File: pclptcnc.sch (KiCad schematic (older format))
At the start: 248 parts, among them P1 ARK825A-3, P3 ARK825A-4, P4 ARK825A-3, P5 ARK825A-3, P6 ARK825A-3, P7 ARK825A-3, P8 ARK825A-3, Q1 BC807-40, Q10 BC807-40, Q11 BC807-40, Q12 BC807-40, Q13 BC807-40, Q14 BC807-40, Q15 BC807-40, Q16 BC807-40, Q17 BC807-40, Q18 BC807-40, Q2 BC807-40, Q3 BC807-40, Q4 BC807-40, Q5 BC807-40, Q6 BC807-40, Q7 BC807-40, Q8 BC807-40, Q9 BC807-40, U1 74LVC1G3157GW, U10 SN74LVC2G17, U11 74HCT14, U12 SN74LVC2G17, U13 74HCT14, U2 HCPL2630, U3 HCPL2630, U4 HCPL2630, U5 HCPL2630, U6 HCPL2630, U7 HCPL2630, U8 74HCT14, U9 74HCT14, j1 DB25, j2 DB25

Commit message: merged all libraries
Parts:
- R1, R10, R100, R101, R102, R103, R104, R105, R106, R107, R108, R109, R11, R110, R111, R112, R113, R114, R115, R116, R117, R118, R119, R12, R120, R121, R122, R123, R13, R14, R15, R16, R17, R18, R19, R2, R20, R21, R22, R23, R24, R25, R26, R27, R28, R29, R3, R30, R31, R32, R33, R34, R35, R36, R37, R38, R39, R4, R40, R41, R42, R43, R44, R45, R46, R47, R48, R49, R5, R50, R51, R52, R53, R54, R55, R56, R57, R58, R59, R6, R60, R61, R62, R63, R64, R65, R66, R67, R68, R69, R7, R70, R71, R72, R73, R74, R75, R76, R77, R78, R79, R8, R80, R81, R82, R83, R84, R85, R86, R87, R88, R89, R9, R90, R91, R92, R93, R94, R95, R96, R97, R98, R99, R_LED1, R_LED10, R_LED11, R_LED12, R_LED13, R_LED14, R_LED15, R_LED16, R_LED17, R_LED18, R_LED19, R_LED2, R_LED20, R_LED3, R_LED4, R_LED5, R_LED6, R_LED7, R_LED8, R_LED9: symbol R -> R_SFP

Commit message: futher library development
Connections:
- no-connect marks 5 -> 7
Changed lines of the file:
@@
 LIBS:valves
 LIBS:new_lib
+LIBS:pclptcnc-cache
 EELAYER 27 0
 EELAYER END
@@
 Sheet 1 1
 Title ""
-Date "1 nov 2013"
+Date "2 nov 2013"
 Rev ""
 Comp ""
@@
 Text Label 19050 6250 0    60   ~ 0
 SENSOR_4
-Text Label 5950 1950 2    60   ~ 0
+Text Label 5950 2000 2    60   ~ 0
 SENSOR_2
 Text Label 10150 2300 0    60   ~ 0
@@
 Text Label 2650 1750 2    60   ~ 0
 RC1
-Text Label 2650 1550 2    60   ~ 0
+Text Label 2650 1500 2    60   ~ 0
 RC2
-Text Label 2650 1950 2    60   ~ 0
+Text Label 2650 2000 2    60   ~ 0
 RC3
-Text Label 2650 2150 2    60   ~ 0
+Text Label 2650 2250 2    60   ~ 0
 RC4
 Text Label 2650 3550 2    60   ~ 0
 RC5
-Text Label 2650 3350 2    60   ~ 0
+Text Label 2650 3300 2    60   ~ 0
 RC6
-Text Label 2650 3750 2    60   ~ 0
+Text Label 2650 3800 2    60   ~ 0
 RC7
-Text Label 2650 3950 2    60   ~ 0
+Text Label 2650 4050 2    60   ~ 0
 RC8
-Text Label 2650 5150 2    60   ~ 0
+Text Label 2650 5100 2    60   ~ 0
 RC9
-Text Label 2650 5550 2    60   ~ 0
+Text Label 2650 5600 2    60   ~ 0
 RC10
 Text Label 2650 5350 2    60   ~ 0
 RC11
-Text Label 2650 5750 2    60   ~ 0
-RC12
 Text Label 2650 5850 2    60   ~ 0
+RC12
+Text Label 2650 5950 2    60   ~ 0
 PC12
 Text Label 2650 5450 2    60   ~ 0
 PC11
-Text Label 2650 5650 2    60   ~ 0
+Text Label 2650 5700 2    60   ~ 0
 PC10
-Text Label 2650 5250 2    60   ~ 0
+Text Label 2650 5200 2    60   ~ 0
 PC9
-Text Label 2650 4050 2    60   ~ 0
+Text Label 2650 4150 2    60   ~ 0
 PC8
-Text Label 2650 3850 2    60   ~ 0
+Text Label 2650 3900 2    60   ~ 0
 PC7
-Text Label 2650 3450 2    60   ~ 0
+Text Label 2650 3400 2    60   ~ 0
 PC6
 Text Label 2650 3650 2    60   ~ 0
 PC5
-Text Label 2650 2250 2    60   ~ 0
+Text Label 2650 2350 2    60   ~ 0
 PC4
-Text Label 2650 2050 2    60   ~ 0
+Text Label 2650 2100 2    60   ~ 0
 PC3
-Text Label 2650 1650 2    60   ~ 0
+Text Label 2650 1600 2    60   ~ 0
 PC2
 Text Label 2650 1850 2    60   ~ 0
@@
 Text Label 5400 9550 0    60   ~ 0
 GND
-Text Label 5950 9950 0    60   ~ 0
+Text Label 6000 9950 0    60   ~ 0
 VCC
 Text Notes 19650 1150 0    60   ~ 0
@@
 Text Label 21900 1450 0    60   ~ 0
 GND
-Text Label 21900 1950 0    60   ~ 0
+Text Label 21900 1550 0    60   ~ 0
 PC_IN1
 Text Label 21900 1750 0    60   ~ 0
 PC_IN2
-Text Label 21900 1550 0    60   ~ 0
+Text Label 21900 1950 0    60   ~ 0
 PC_IN3
 Text Label 21900 1350 0    60   ~ 0
@@
 Text Label 20400 6250 0    60   ~ 0
 SENSOR_5
-Text Label 5950 1550 2    60   ~ 0
+Text Label 5950 1500 2    60   ~ 0
 SENSOR_4
-Text Label 5950 2150 2    60   ~ 0
+Text Label 5950 2250 2    60   ~ 0
 SENSOR_1
 Text Label 20100 5950 0    60   ~ 0
@@
 Text Label 13050 2600 0    60   ~ 0
 ISOLATED_GND
-Text Label 13050 1700 0    60   ~ 0
-ISOLATED_VCC
 $Comp
 L HCPL2630 U4
@@
 Text Notes 16950 4350 0    60   ~ 0
 OUTPUT CONNECTORS
-Text Label 6150 7050 0    60   ~ 0
+Text Label 6250 7050 0    60   ~ 0
 ISOLATED_VCC
-Text Label 5350 7450 0    60   ~ 0
+Text Label 5300 7450 0    60   ~ 0
 ISOLATED_GND
 Text Label 10250 6500 0    60   ~ 0
@@
 	18800 5300 18800 4900
 Wire Wire Line
-	19050 4500 18550 4500
+	18550 4500 19050 4500
 Wire Wire Line
 	18750 5650 18750 5850
@@
 	21500 5300 21500 4900
 Wire Wire Line
-	21750 4500 21250 4500
+	21250 4500 21750 4500
 Wire Wire Line
 	21450 5650 21450 5850
@@
 	20150 5300 20150 4900
 Wire Wire Line
-	20400 4500 19900 4500
+	19900 4500 20400 4500
 Wire Wire Line
 	20100 5650 20100 5850
@@
 	18800 7050 18800 6650
 Wire Wire Line
-	19050 6250 18550 6250
+	18550 6250 19050 6250
 Wire Wire Line
 	18750 7400 18750 7600
@@
 	20150 7050 20150 6650
 Wire Wire Line
-	20400 6250 19900 6250
+	19900 6250 20400 6250
 Wire Wire Line
 	20100 7400 20100 7600
@@
 	5150 7050 5450 7050
 Wire Wire Line
-	5400 9550 6600 9550
+	6600 9550 5400 9550
 Connection ~ 6200 9550
 Wire Wire Line
-	6600 9550 6600 8850
+	6600 8850 6600 9550
 Connection ~ 6600 9200
 Wire Wire Line
@@
 Connection ~ 7000 9550
 Connection ~ 6600 9950
-Wire Wire Line
-	5200 9950 5200 9550
 Connection ~ 6200 9950
 Wire Wire Line
@@
 Text Label 20250 3650 0    60   ~ 0
 SENSOR_5
-Text Label 5200 9950 0    60   ~ 0
-VCC_NFused
-$Comp
-L FUSE_N F1
-U 1 1 523251F3
-P 5700 7050
-F 0 "F1" H 5800 7100 40  0000 C CNN
-F 1 "FUSE 1A" H 5600 7000 40  0000 C CNN
-F 2 "~" H 5700 7050 60  0000 C CNN
-F 3 "~" H 5700 7050 60  0000 C CNN
-	1    5700 7050
-	1    0    0    -1
-$EndComp
-$Comp
-L FUSE_N F2
-U 1 1 523253C0
-P 5700 9950
-F 0 "F2" H 5800 10000 40  0000 C CNN
-F 1 "FUSE 0.5A" H 5600 9900 40  0000 C CNN
-F 2 "~" H 5700 9950 60  0000 C CNN
-F 3 "~" H 5700 9950 60  0000 C CNN
-	1    5700 9950
-	1    0    0    -1
-$EndComp
-Text Label 5200 7050 0    60   ~ 0
+Text Label 5150 7050 0    60   ~ 0
 ISOLATED_VCC_NFused
 NoConn ~ 5150 7250
-Text Label 5950 2250 2    60   ~ 0
+Text Label 5950 2350 2    60   ~ 0
 GND
 Text Label 5950 3550 2    60   ~ 0
@@
 Text Label 5700 5950 0    60   ~ 0
 IOSRCTR_BASE
-Text Label 5950 2050 2    60   ~ 0
+Text Label 5950 2100 2    60   ~ 0
 GND
 Text Label 5950 1850 2    60   ~ 0
 GND
-Text Label 5950 1650 2    60   ~ 0
+Text Label 5950 1600 2    60   ~ 0
 GND
 $Comp
@@
 Text Label 10100 11500 2    60   ~ 0
 SRC_SEL
+Text Label 5250 9950 0    60   ~ 0
+VCC_NFused
+Wire Wire Line
+	5200 9950 5200 9550
+NoConn ~ 12100 10750
+NoConn ~ 12100 10950
+Text Label 13050 1700 0    60   ~ 0
+ISOLATED_VCC
+$Comp
+L FUSE_N F1
+U 1 1 52754D48
+P 5700 7050
+F 0 "F1" H 5800 7100 40  0000 C CNN
+F 1 "FUSE 1A" H 5600 7000 40  0000 C CNN
+F 2 "~" H 5700 7050 60  0000 C CNN
+F 3 "~" H 5700 7050 60  0000 C CNN
+	1    5700 7050
+	1    0    0    -1
+$EndComp
+$Comp
+L FUSE_N F2
+U 1 1 52754D55
+P 5700 9950
+F 0 "F2" H 5800 10000 40  0000 C CNN
+F 1 "FUSE 0.5A" H 5600 9900 40  0000 C CNN
+F 2 "~" H 5700 9950 60  0000 C CNN
+F 3 "~" H 5700 9950 60  0000 C CNN
+	1    5700 9950
+	1    0    0    -1
+$EndComp
 $EndSCHEMATC

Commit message: 05.11.1305.11.1305.11.1305.11.1305.11.13
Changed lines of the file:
@@
 Text Label 5950 3850 2    60   ~ 0
 SENSOR_5
-Text Label 5950 1750 2    60   ~ 0
+Text Label 5950 2000 2    60   ~ 0
 SENSOR_3
 Text Label 19050 6250 0    60   ~ 0
 SENSOR_4
-Text Label 5950 2000 2    60   ~ 0
+Text Label 5950 1750 2    60   ~ 0
 SENSOR_2
 Text Label 10150 2300 0    60   ~ 0
@@
 Text Label 19200 9800 0    60   ~ 0
 PC12
-Text Label 2650 1750 2    60   ~ 0
+Text Label 2650 2000 2    60   ~ 0
 RC1
 Text Label 2650 1500 2    60   ~ 0
 RC2
-Text Label 2650 2000 2    60   ~ 0
+Text Label 2650 1750 2    60   ~ 0
 RC3
 Text Label 2650 2250 2    60   ~ 0
@@
 Text Label 2650 2350 2    60   ~ 0
 PC4
-Text Label 2650 2100 2    60   ~ 0
+Text Label 2650 1850 2    60   ~ 0
 PC3
 Text Label 2650 1600 2    60   ~ 0
 PC2
-Text Label 2650 1850 2    60   ~ 0
+Text Label 2650 2100 2    60   ~ 0
 PC1
 $Comp

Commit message: huge optocouplers movement
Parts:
- removed MUX1, MUX2, MUX3, MUX4: 74HC158, SO16E, symbol 74LS158
- added MUX1, MUX2, MUX3, MUX4: 74HC158, ~, symbol 74HC158
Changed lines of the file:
@@
 Sheet 1 1
 Title ""
-Date "2 nov 2013"
+Date "5 nov 2013"
 Rev ""
 Comp ""
@@
 Text Label 5950 3850 2    60   ~ 0
 SENSOR_5
-Text Label 5950 2000 2    60   ~ 0
+Text Label 5950 1950 2    60   ~ 0
 SENSOR_3
 Text Label 19050 6250 0    60   ~ 0
@@
 $EndComp
 $Comp
-L 74LS158 MUX1
-U 1 1 522E2A35
-P 3400 2050
-F 0 "MUX1" H 3450 2200 60  0000 C CNN
-F 1 "74HC158" H 3450 1900 60  0000 C CNN
-F 2 "SO16E" H 3400 2050 60  0000 C CNN
-F 3 "~" H 3400 2050 60  0000 C CNN
-	1    3400 2050
-	1    0    0    -1
-$EndComp
-$Comp
-L 74LS158 MUX2
-U 1 1 522E2A36
-P 3400 3850
-F 0 "MUX2" H 3450 4000 60  0000 C CNN
-F 1 "74HC158" H 3450 3700 60  0000 C CNN
-F 2 "SO16E" H 3400 3850 60  0000 C CNN
-F 3 "~" H 3400 3850 60  0000 C CNN
-	1    3400 3850
-	1    0    0    -1
-$EndComp
-$Comp
 L 74HCT14 U8
 U 1 1 522E2A37
@@
 Text Label 19200 10800 0    60   ~ 0
 PC7
-Text Label 21850 10800 0    60   ~ 0
-PC8
 Text Label 21850 10600 0    60   ~ 0
+PC8
+Text Label 21850 10800 0    60   ~ 0
 PC9
 Text Label 21850 8800 0    60   ~ 0
@@
 Text Label 19200 9800 0    60   ~ 0
 PC12
-Text Label 2650 2000 2    60   ~ 0
+Text Label 2650 2150 2    60   ~ 0
 RC1
-Text Label 2650 1500 2    60   ~ 0
+Text Label 2650 1950 2    60   ~ 0
 RC2
 Text Label 2650 1750 2    60   ~ 0
 RC3
-Text Label 2650 2250 2    60   ~ 0
+Text Label 2650 1550 2    60   ~ 0
 RC4
-Text Label 2650 3550 2    60   ~ 0
+Text Label 2650 5150 2    60   ~ 0
 RC5
-Text Label 2650 3300 2    60   ~ 0
+Text Label 2650 3350 2    60   ~ 0
 RC6
-Text Label 2650 3800 2    60   ~ 0
+Text Label 2650 3750 2    60   ~ 0
 RC7
-Text Label 2650 4050 2    60   ~ 0
+Text Label 2650 5350 2    60   ~ 0
 RC8
-Text Label 2650 5100 2    60   ~ 0
+Text Label 2650 3550 2    60   ~ 0
 RC9
-Text Label 2650 5600 2    60   ~ 0
+Text Label 2650 5750 2    60   ~ 0
 RC10
-Text Label 2650 5350 2    60   ~ 0
+Text Label 2650 3950 2    60   ~ 0
 RC11
-Text Label 2650 5850 2    60   ~ 0
+Text Label 2650 5550 2    60   ~ 0
 RC12
-Text Label 2650 5950 2    60   ~ 0
+Text Label 2650 4050 2    60   ~ 0
 PC12
-Text Label 2650 5450 2    60   ~ 0
+Text Label 2650 5650 2    60   ~ 0
 PC11
-Text Label 2650 5700 2    60   ~ 0
+Text Label 2650 5850 2    60   ~ 0
 PC10
-Text Label 2650 5200 2    60   ~ 0
+Text Label 2650 5250 2    60   ~ 0
 PC9
-Text Label 2650 4150 2    60   ~ 0
+Text Label 2650 5450 2    60   ~ 0
 PC8
-Text Label 2650 3900 2    60   ~ 0
+Text Label 2650 3850 2    60   ~ 0
 PC7
-Text Label 2650 3400 2    60   ~ 0
+Text Label 2650 3450 2    60   ~ 0
 PC6
 Text Label 2650 3650 2    60   ~ 0
 PC5
-Text Label 2650 2350 2    60   ~ 0
+Text Label 2650 2250 2    60   ~ 0
 PC4
 Text Label 2650 1850 2    60   ~ 0
 PC3
-Text Label 2650 1600 2    60   ~ 0
+Text Label 2650 1650 2    60   ~ 0
 PC2
-Text Label 2650 2100 2    60   ~ 0
+Text Label 2650 2050 2    60   ~ 0
 PC1
 $Comp
@@
 Text Label 6000 6150 3    60   ~ 0
 VCC
-Text Label 15150 9400 2    60   ~ 0
+Text Label 15150 9200 2    60   ~ 0
 RCOUT1
-Text Label 15150 9600 2    60   ~ 0
+Text Label 15150 9000 2    60   ~ 0
 RCOUT2
-Text Label 15150 9800 2    60   ~ 0
-RCOUT3
 Text Label 15150 8800 2    60   ~ 0
+RCOUT3
+Text Label 15150 9400 2    60   ~ 0
 RCOUT4
-Text Label 15150 9000 2    60   ~ 0
+Text Label 15150 9600 2    60   ~ 0
 RCOUT5
-Text Label 15150 9200 2    60   ~ 0
+Text Label 15150 9800 2    60   ~ 0
 RCOUT6
 Text Label 15150 11200 2    60   ~ 0
@@
 Text Label 15150 11600 2    60   ~ 0
 RCOUT9
-Text Label 15150 10600 2    60   ~ 0
+Text Label 15150 11000 2    60   ~ 0
 RCOUT10
 Text Label 15150 10800 2    60   ~ 0
 RCOUT11
-Text Label 15150 11000 2    60   ~ 0
+Text Label 15150 10600 2    60   ~ 0
 RCOUT12
 Text Label 6800 5750 0    60   ~ 0
@@
 Text Label 5700 5550 2    60   ~ 0
 CTRL_SRC
-$Comp
-L 74LS158 MUX3
-U 1 1 522E2A4E
-P 3400 5650
-F 0 "MUX3" H 3450 5800 60  0000 C CNN
-F 1 "74HC158" H 3450 5500 60  0000 C CNN
-F 2 "SO16E" H 3400 5650 60  0000 C CNN
-F 3 "~" H 3400 5650 60  0000 C CNN
-	1    3400 5650
-	1    0    0    -1
-$EndComp
 Text Label 2650 6200 2    60   ~ 0
 GND
@@
 Text Label 17700 10600 2    60   ~ 0
 PC_OUT_A6
-Text Label 17700 11600 2    60   ~ 0
+Text Label 17700 11200 2    60   ~ 0
 PC_OUT_A7
 Text Label 21900 2850 0    60   ~ 0
@@
 Text Label 17700 11400 2    60   ~ 0
 PC_OUT_A8
-Text Label 17700 11200 2    60   ~ 0
+Text Label 17700 11600 2    60   ~ 0
 PC_OUT_A9
 Text Label 20350 8800 2    60   ~ 0
@@
 Text Label 20400 6250 0    60   ~ 0
 SENSOR_5
-Text Label 5950 1500 2    60   ~ 0
+Text Label 5950 1550 2    60   ~ 0
 SENSOR_4
-Text Label 5950 2250 2    60   ~ 0
+Text Label 5950 2150 2    60   ~ 0
 SENSOR_1
 Text Label 20100 5950 0    60   ~ 0
@@
 Text Label 3600 6450 0    60   ~ 0
 GND
-Text Label 4150 1550 0    60   ~ 0
+Text Label 4150 2300 0    60   ~ 0
 FLTRD_SGNL1
-Text Label 4150 2050 0    60   ~ 0
-FLTRD_SGNL2
 Text Label 4150 1800 0    60   ~ 0
+FLTRD_SGNL2
+Text Label 4150 2050 0    60   ~ 0
 FLTRD_SGNL3
-Text Label 4150 2300 0    60   ~ 0
+Text Label 4150 1550 0    60   ~ 0
 FLTRD_SGNL4
 Text Label 4150 3350 0    60   ~ 0
@@
 ISOLATED_VCC_NFused
 NoConn ~ 5150 7250
-Text Label 5950 2350 2    60   ~ 0
+Text Label 5950 2250 2    60   ~ 0
 GND
 Text Label 5950 3550 2    60   ~ 0
@@
 Text Label 5700 5950 0    60   ~ 0
 IOSRCTR_BASE
-Text Label 5950 2100 2    60   ~ 0
+Text Label 5950 2050 2    60   ~ 0
 GND
 Text Label 5950 1850 2    60   ~ 0
 GND
-Text Label 5950 1600 2    60   ~ 0
+Text Label 5950 1650 2    60   ~ 0
 GND
 $Comp
@@
 Text Label 5700 6350 2    60   ~ 0
 GND
-$Comp
-L 74LS158 MUX4
-U 1 1 526D4CB1
-P 6700 2050
-F 0 "MUX4" H 6750 2200 60  0000 C CNN
-F 1 "74HC158" H 6750 1900 60  0000 C CNN
-F 2 "SO16E" H 6700 2050 60  0000 C CNN
-F 3 "~" H 6700 2050 60  0000 C CNN
-	1    6700 2050
-	1    0    0    -1
-$EndComp
 NoConn ~ 21850 11400
 NoConn ~ 20350 11400
@@
 	1    0    0    -1
 $EndComp
+Text Label 5800 9350 0    60   ~ 0
+ISOLATED_VCC
+Text Label 6100 9350 0    60   ~ 0
+ISOLATED_GND
+$Comp
+L 74HC158 MUX1
+U 1 1 5278E1DD
+P 3400 2050
+F 0 "MUX1" H 3450 2200 60  0000 C CNN
+F 1 "74HC158" H 3450 1900 60  0000 C CNN
+F 2 "~" H 3400 2050 60  0000 C CNN
+F 3 "~" H 3400 2050 60  0000 C CNN
+	1    3400 2050
+	1    0    0    -1
+$EndComp
+$Comp
+L 74HC158 MUX2
+U 1 1 5278E1EA
+P 3400 3850
+F 0 "MUX2" H 3450 4000 60  0000 C CNN
+F 1 "74HC158" H 3450 3700 60  0000 C CNN
+F 2 "~" H 3400 3850 60  0000 C CNN
+F 3 "~" H 3400 3850 60  0000 C CNN
+	1    3400 3850
+	1    0    0    -1
+$EndComp
+$Comp
+L 74HC158 MUX3
+U 1 1 5278E1F0
+P 3400 5650
+F 0 "MUX3" H 3450 5800 60  0000 C CNN
+F 1 "74HC158" H 3450 5500 60  0000 C CNN
+F 2 "~" H 3400 5650 60  0000 C CNN
+F 3 "~" H 3400 5650 60  0000 C CNN
+	1    3400 5650
+	1    0    0    -1
+$EndComp
+$Comp
+L 74HC158 MUX4
+U 1 1 5278E1F6
+P 6700 2050
+F 0 "MUX4" H 6750 2200 60  0000 C CNN
+F 1 "74HC158" H 6750 1900 60  0000 C CNN
+F 2 "~" H 6700 2050 60  0000 C CNN
+F 3 "~" H 6700 2050 60  0000 C CNN
+	1    6700 2050
+	1    0    0    -1
+$EndComp

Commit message: близкая компоновка
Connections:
- net FLTRD_SGNL11: now also MUX3.9 (Zd); no longer MUX3.7 (Zb)
- net FLTRD_SGNL12: now also MUX3.7 (Zb); no longer MUX3.9 (Zd)
- net FLTRD_SGNL5: now also MUX2.9 (Zd); no longer MUX2.4 (Za)
- net FLTRD_SGNL6: now also MUX2.7 (Zb); no longer MUX2.12 (Zc)
- net FLTRD_SGNL7: now also MUX2.12 (Zc); no longer MUX2.7 (Zb)
- net FLTRD_SGNL8: now also MUX2.4 (Za); no longer MUX2.9 (Zd)
- net PC12: now also U11.6 (3Y); no longer U10.4 (2Y)
- net PC4: now also U10.4 (2Y); no longer U11.2 (1Y)
- net PC5: now also MUX2.13 (I1c); no longer MUX2.6 (I1b)
- net PC6: now also MUX2.6 (I1b), U11.2 (1Y); no longer MUX2.3 (I1a), U11.6 (3Y)
- net PC7: now also MUX2.3 (I1a); no longer MUX2.13 (I1c)
- net RC11: now also MUX2.2 (I0a); no longer MUX2.11 (I0d)
- net RC6: now also MUX2.14 (I0c); no longer MUX2.2 (I0a)
- net RC7: now also MUX2.11 (I0d); no longer MUX2.14 (I0c)
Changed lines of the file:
@@
 Sheet 1 1
 Title ""
-Date "5 nov 2013"
+Date "6 nov 2013"
 Rev ""
 Comp ""
@@
 Text Label 19200 11600 0    60   ~ 0
 PC3
-Text Label 19200 10600 0    60   ~ 0
+Text Label 19200 9800 0    60   ~ 0
 PC4
 Text Label 21850 11000 0    60   ~ 0
 PC5
-Text Label 19200 11000 0    60   ~ 0
+Text Label 19200 10600 0    60   ~ 0
 PC6
 Text Label 19200 10800 0    60   ~ 0
@@
 Text Label 21850 9800 0    60   ~ 0
 PC11
-Text Label 19200 9800 0    60   ~ 0
+Text Label 19200 11000 0    60   ~ 0
 PC12
 Text Label 2650 2150 2    60   ~ 0
@@
 Text Label 2650 5150 2    60   ~ 0
 RC5
-Text Label 2650 3350 2    60   ~ 0
+Text Label 2650 3750 2    60   ~ 0
 RC6
-Text Label 2650 3750 2    60   ~ 0
+Text Label 2650 3950 2    60   ~ 0
 RC7
 Text Label 2650 5350 2    60   ~ 0
@@
 Text Label 2650 5750 2    60   ~ 0
 RC10
-Text Label 2650 3950 2    60   ~ 0
+Text Label 2650 3350 2    60   ~ 0
 RC11
 Text Label 2650 5550 2    60   ~ 0
@@
 Text Label 2650 5450 2    60   ~ 0
 PC8
+Text Label 2650 3450 2    60   ~ 0
+PC7
+Text Label 2650 3650 2    60   ~ 0
+PC6
 Text Label 2650 3850 2    60   ~ 0
-PC7
-Text Label 2650 3450 2    60   ~ 0
-PC6
-Text Label 2650 3650 2    60   ~ 0
 PC5
 Text Label 2650 2250 2    60   ~ 0
@@
 Text Label 4150 1550 0    60   ~ 0
 FLTRD_SGNL4
+Text Label 4150 4100 0    60   ~ 0
+FLTRD_SGNL5
+Text Label 4150 3600 0    60   ~ 0
+FLTRD_SGNL6
+Text Label 4150 3850 0    60   ~ 0
+FLTRD_SGNL7
 Text Label 4150 3350 0    60   ~ 0
-FLTRD_SGNL5
-Text Label 4150 3850 0    60   ~ 0
-FLTRD_SGNL6
-Text Label 4150 3600 0    60   ~ 0
-FLTRD_SGNL7
-Text Label 4150 4100 0    60   ~ 0
 FLTRD_SGNL8
 Text Label 4150 5150 0    60   ~ 0
@@
 Text Label 4150 5650 0    60   ~ 0
 FLTRD_SGNL10
+Text Label 4150 5900 0    60   ~ 0
+FLTRD_SGNL11
 Text Label 4150 5400 0    60   ~ 0
-FLTRD_SGNL11
-Text Label 4150 5900 0    60   ~ 0
 FLTRD_SGNL12
 Text Label 7450 1800 0    60   ~ 0

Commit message: version 0.2a completed
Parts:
- removed R1: 2K7, SM0805, symbol R_SFP
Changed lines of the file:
@@
 Text Label 5950 4150 2    60   ~ 0
 RC_SW_INV
-$Comp
-L BC807-40 Q1
-U 1 1 526C7C8B
-P 5900 5950
-F 0 "Q1" V 6150 6000 40  0000 R CNN
-F 1 "BC807-40" H 5900 6100 40  0000 R CNN
-F 2 "SOT23" H 5700 6052 29  0000 C CNN
-F 3 "~" H 5900 5950 60  0000 C CNN
-	1    5900 5950
-	1    0    0    -1
-$EndComp
-$Comp
-L R_SFP R1
-U 1 1 526C7CA0
-P 5700 6150
-F 0 "R1" V 5780 6150 40  0000 C CNN
-F 1 "2K7" V 5707 6151 40  0000 C CNN
-F 2 "SM0805" V 5630 6150 30  0000 C CNN
-F 3 "~" H 5700 6150 30  0000 C CNN
-	1    5700 6150
-	-1   0    0    -1
-$EndComp
-Text Label 5700 6350 2    60   ~ 0
-GND
 NoConn ~ 21850 11400
 NoConn ~ 20350 11400
@@
 	1    0    0    -1
 $EndComp
+$Comp
+L BC807-40 Q1
+U 1 1 526C7C8B
+P 5900 5950
+F 0 "Q1" V 6150 6000 40  0000 R CNN
+F 1 "BC807-40" H 5900 6100 40  0000 R CNN
+F 2 "SOT23" H 5700 6052 29  0000 C CNN
+F 3 "~" H 5900 5950 60  0000 C CNN
+	1    5900 5950
+	1    0    0    -1
+$EndComp

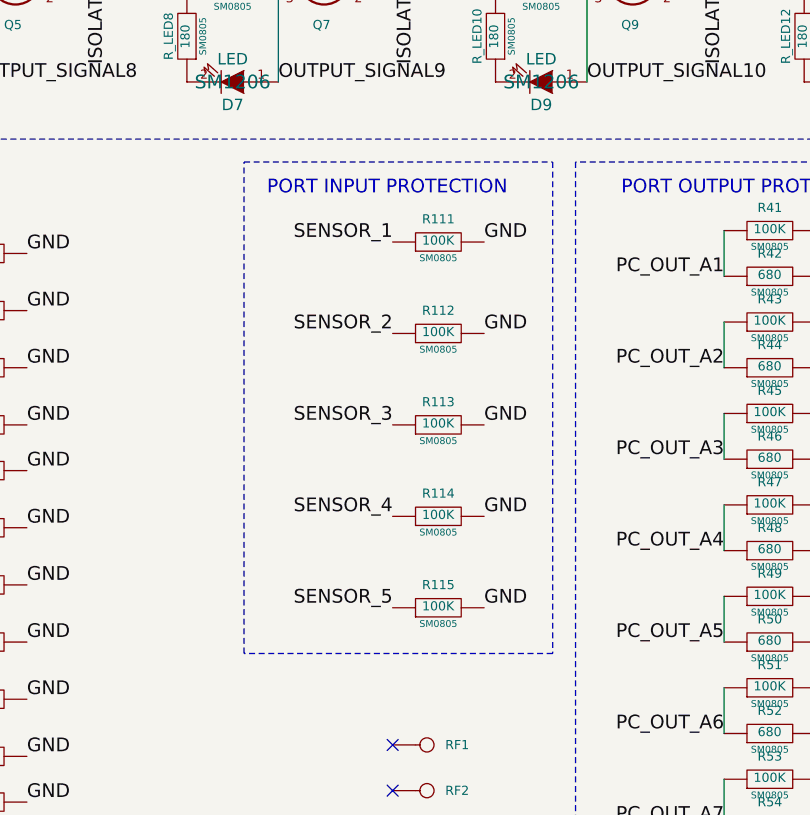
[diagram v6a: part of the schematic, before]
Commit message: odd komponents removed
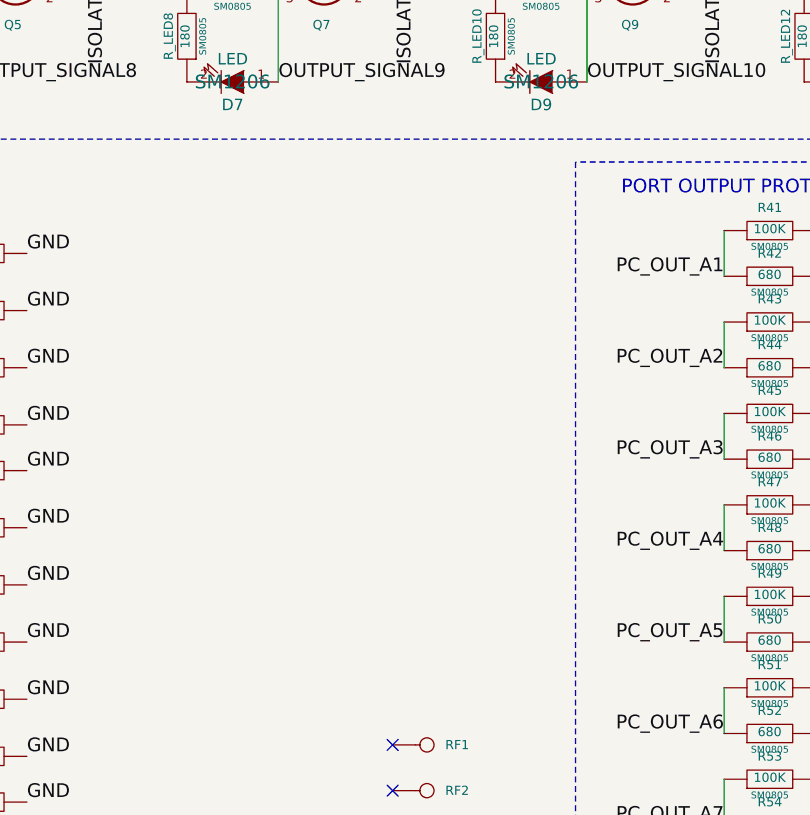
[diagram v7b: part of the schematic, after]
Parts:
- removed R111, R112, R113, R114, R115: 100K, SM0805, symbol R_SFP
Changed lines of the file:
@@
 Sheet 1 1
 Title ""
-Date "6 nov 2013"
+Date "7 nov 2013"
 Rev ""
 Comp ""
@@
 PC_IN_A2
 $Comp
-L R_SFP R111
-U 1 1 526D9D3C
-P 12300 8550
-F 0 "R111" V 12400 8550 40  0000 C CNN
-F 1 "100K" V 12307 8551 40  0000 C CNN
-F 2 "SM0805" V 12230 8550 30  0000 C CNN
-F 3 "~" H 12300 8550 30  0000 C CNN
-	1    12300 8550
-	0    -1   -1   0
-$EndComp
-Text Label 12500 8550 0    60   ~ 0
-GND
-Text Notes 11550 8350 0    60   ~ 0
-PORT INPUT PROTECTION
-$Comp
-L R_SFP R112
-U 1 1 526D9D4C
-P 12300 8950
-F 0 "R112" V 12400 8950 40  0000 C CNN
-F 1 "100K" V 12307 8951 40  0000 C CNN
-F 2 "SM0805" V 12230 8950 30  0000 C CNN
-F 3 "~" H 12300 8950 30  0000 C CNN
-	1    12300 8950
-	0    -1   -1   0
-$EndComp
-Text Label 12500 8950 0    60   ~ 0
-GND
-Text Label 12500 9350 0    60   ~ 0
-GND
-$Comp
-L R_SFP R114
-U 1 1 526D9D6A
-P 12300 9750
-F 0 "R114" V 12400 9750 40  0000 C CNN
-F 1 "100K" V 12307 9751 40  0000 C CNN
-F 2 "SM0805" V 12230 9750 30  0000 C CNN
-F 3 "~" H 12300 9750 30  0000 C CNN
-	1    12300 9750
-	0    -1   -1   0
-$EndComp
-Text Label 12500 9750 0    60   ~ 0
-GND
-$Comp
-L R_SFP R115
-U 1 1 526D9D79
-P 12300 10150
-F 0 "R115" V 12400 10150 40  0000 C CNN
-F 1 "100K" V 12307 10151 40  0000 C CNN
-F 2 "SM0805" V 12230 10150 30  0000 C CNN
-F 3 "~" H 12300 10150 30  0000 C CNN
-	1    12300 10150
-	0    -1   -1   0
-$EndComp
-Text Label 12500 10150 0    60   ~ 0
-GND
-Wire Notes Line
-	12800 8200 12800 10350
-Wire Notes Line
-	12800 10350 11450 10350
-Wire Notes Line
-	11450 10350 11450 8200
-Wire Notes Line
-	11450 8200 12800 8200
-$Comp
-L R_SFP R113
-U 1 1 526D9D5B
-P 12300 9350
-F 0 "R113" V 12400 9350 40  0000 C CNN
-F 1 "100K" V 12307 9351 40  0000 C CNN
-F 2 "SM0805" V 12230 9350 30  0000 C CNN
-F 3 "~" H 12300 9350 30  0000 C CNN
-	1    12300 9350
-	0    -1   -1   0
-$EndComp
-Text Label 12100 8550 2    60   ~ 0
-SENSOR_1
-Text Label 12100 8950 2    60   ~ 0
-SENSOR_2
-Text Label 12100 9350 2    60   ~ 0
-SENSOR_3
-Text Label 12100 9750 2    60   ~ 0
-SENSOR_4
-Text Label 12100 10150 2    60   ~ 0
-SENSOR_5
-$Comp
 L R_SFP R7
